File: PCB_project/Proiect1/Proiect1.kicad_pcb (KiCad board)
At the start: 2 copper layers, 40 x 40 mm, 39 parts, among them J1 Out, J2 GND, J3 Vcc, J4 GND, Q1 BC846, Q10 BC846, Q11 BC846, Q12 BC856, Q13 BC856, Q2 BC856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

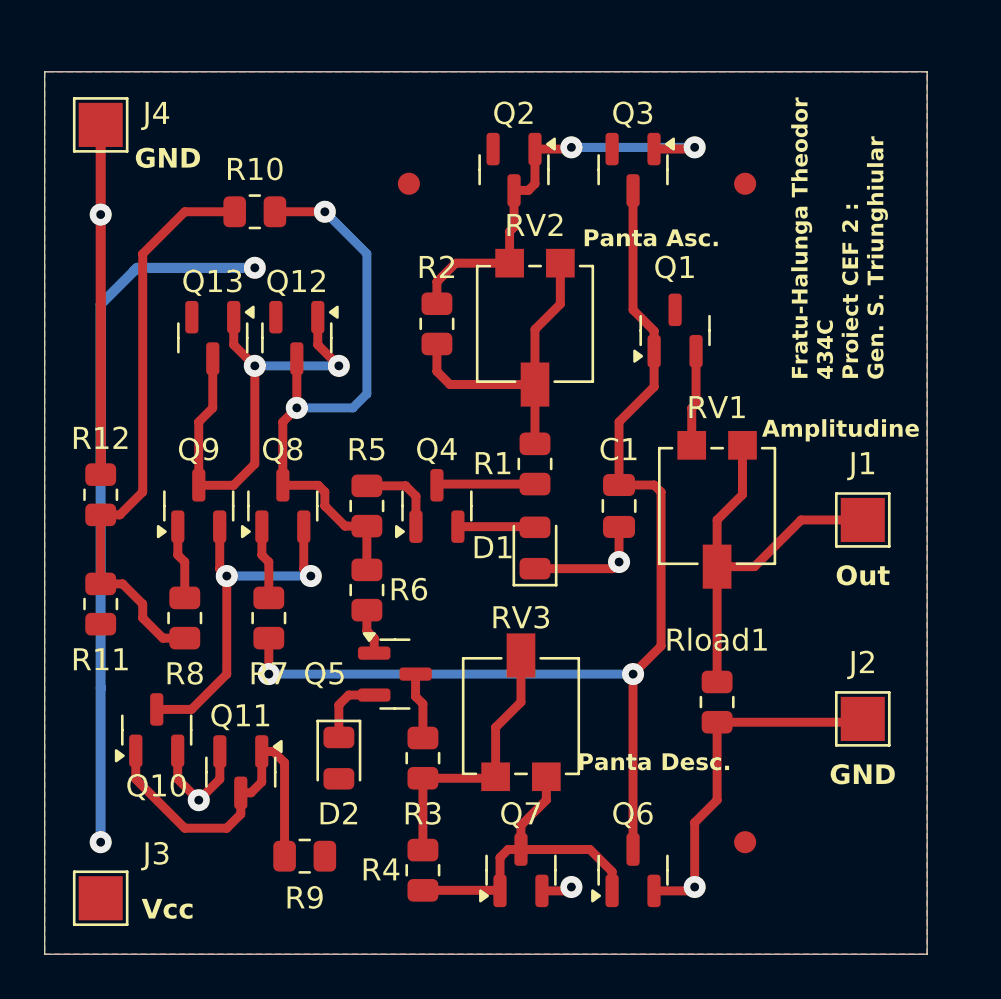
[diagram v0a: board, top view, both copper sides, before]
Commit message: Fixed some alignment issues
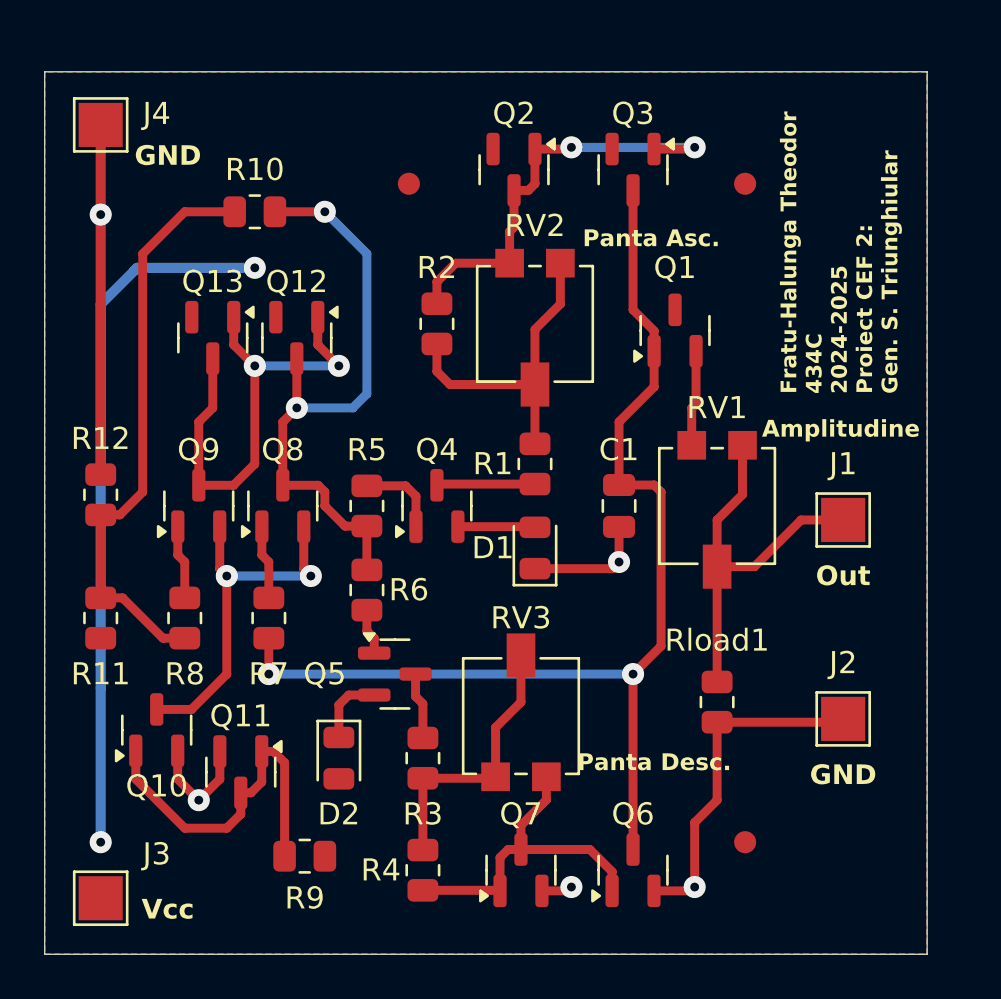
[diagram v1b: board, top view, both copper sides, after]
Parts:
- moved J1 0.89 mm to (97.7, 95.3)
- moved J2 0.89 mm to (97.7, 104.3)
- moved R11 0.64 mm to (64.0, 99.8)
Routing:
- net Net-(J1-Pin_1): track 18.7 -> 17.8 mm
- net GND: track 44.5 -> 43.6 mm
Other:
- board text added: "Fratu-Halunga Theodor 434C 2024-2025 Proiect CEF 2: Gen. S. Triunghiular"
- board text removed: "Fratu-Halunga Theodor 434C Proiect CEF 2 : Gen. S. Triunghiular"
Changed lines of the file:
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@@
 	(footprint "TestPoint:TestPoint_Pad_2.0x2.0mm"
 		(layer "F.Cu")
-		(at 98.584 104.332)
+		(at 97.695 104.332)
 		(descr "SMD rectangular pad as test Point, square 2.0mm side length")
 		(tags "test point SMD pad rectangle square")
@@
 	(footprint "TestPoint:TestPoint_Pad_2.0x2.0mm"
 		(layer "F.Cu")
-		(at 98.584 95.315)
+		(at 97.695 95.315)
 		(descr "SMD rectangular pad as test Point, square 2.0mm side length")
 		(tags "test point SMD pad rectangle square")
@@
 	(footprint "Resistor_SMD:R_0805_2012Metric"
 		(layer "F.Cu")
-		(at 64.04 99.125 -90)
+		(at 64.04 99.76 -90)
 		(descr "Resistor SMD 0805 (2012 Metric), square (rectangular) end terminal, IPC_7351 nominal, (Body size source: IPC-SM-782 page 72, https://www.pcb-3d.com/wordpress/wp-content/uploads/ipc-sm-782a_amendment_1_and_2.pdf), generated with kicad-footprint-generator")
 		(tags "resistor")
@@
 		)
 		(property "Value" "GND"
-			(at 3.048 1.524 0)
+			(at 3.048 1.397 0)
 			(layer "F.SilkS" knockout)
 			(effects
@@
 		)
 	)
-	(gr_text "Fratu-Halunga Theodor\n434C\nProiect CEF 2 : \nGen. S. Triunghiular"
-		(at 99.6 88.965 90)
+	(gr_text "Fratu-Halunga Theodor\n434C\n2024-2025\nProiect CEF 2: \nGen. S. Triunghiular"
+		(at 100.235 89.6 90)
 		(layer "F.SilkS" knockout)
 		(effects
@@
 	)
 	(segment
-		(start 98.4335 104.4825)
-		(end 98.584 104.332)
-		(width 0.4064)
-		(layer "F.Cu")
-		(net 2)
-	)
-	(segment
 		(start 67.53 107.06)
 		(end 68.485 108.015)
@@
 	)
 	(segment
-		(start 91.98 104.4825)
-		(end 98.4335 104.4825)
+		(start 69.44 107.06)
+		(end 68.485 108.015)
 		(width 0.4064)
 		(layer "F.Cu")
@@
 	)
 	(segment
-		(start 69.44 107.06)
-		(end 68.485 108.015)
+		(start 87.535 95.63)
+		(end 87.535 97.22)
 		(width 0.4064)
 		(layer "F.Cu")
@@
 	)
 	(segment
-		(start 87.535 95.63)
-		(end 87.535 97.22)
+		(start 91.98 104.4825)
+		(end 97.5445 104.4825)
 		(width 0.4064)
 		(layer "F.Cu")
@@
 		(net 2)
 	)
+	(segment
+		(start 97.5445 104.4825)
+		(end 97.695 104.332)
+		(width 0.4064)
+		(layer "F.Cu")
+		(net 2)
+	)
 	(via
 		(at 87.535 97.22)
@@
 	)
 	(segment
-		(start 91.98 97.43)
-		(end 93.675 97.43)
+		(start 95.79 95.315)
+		(end 97.695 95.315)
 		(width 0.4064)
 		(layer "F.Cu")
@@
 	)
 	(segment
-		(start 91.98 102.6575)
-		(end 91.98 97.43)
+		(start 91.98 97.43)
+		(end 93.675 97.43)
 		(width 0.4064)
 		(layer "F.Cu")
@@
 	)
 	(segment
-		(start 95.79 95.315)
-		(end 98.584 95.315)
+		(start 91.98 102.6575)
+		(end 91.98 97.43)
 		(width 0.4064)
 		(layer "F.Cu")
@@
 	)
 	(segment
-		(start 67.85 100.6725)
+		(start 65.0325 98.8475)
 		(end 66.8575 100.6725)
 		(width 0.4064)
@@
 	)
 	(segment
-		(start 65.945 99.76)
-		(end 65.945 99.125)
-		(width 0.4064)
-		(layer "F.Cu")
-		(net 22)
-	)
-	(segment
-		(start 65.0325 98.2125)
-		(end 64.04 98.2125)
+		(start 64.04 98.8475)
+		(end 65.0325 98.8475)
 		(width 0.4064)
 		(layer "F.Cu")
@@
 	)
 	(segment
-		(start 65.945 99.125)
-		(end 65.0325 98.2125)
+		(start 66.8575 100.6725)
+		(end 67.85 100.6725)
 		(width 0.4064)
 		(layer "F.Cu")
@@
 	)
 	(segment
-		(start 64.9055 95.0845)
-		(end 65.945 94.045)
+		(start 64.04 95.0845)
+		(end 64.04 98.8475)
 		(width 0.4064)
 		(layer "F.Cu")
@@
 	)
 	(segment
-		(start 66.8575 100.6725)
-		(end 65.945 99.76)
+		(start 64.9055 95.0845)
+		(end 65.945 94.045)
 		(width 0.4064)
 		(layer "F.Cu")
@@
 		(width 0.4064)
 		(layer "F.Cu")
-		(net 22)
-	)
-	(segment
-		(start 64.04 98.2125)
-		(end 64.04 95.0845)
-		(width 0.4064)
-		(layer "F.Cu")

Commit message: Created Gerber files
Also moved the stackup and the drill map on the same layer, because apparently KiCad can't export multiple layers in the same Gerber file.
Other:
- board text added: "Dielectric"
- board text removed: "Dielectric 1"
